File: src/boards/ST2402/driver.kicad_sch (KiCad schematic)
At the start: 61 parts, among them J15 Screw_Terminal_01x01, J16 Screw_Terminal_01x01, J17 Screw_Terminal_01x01, J9 Screw_Terminal_01x02, Q1 STB100N10F7, Q2 STB100N10F7, U2 LM317L_SOT-89

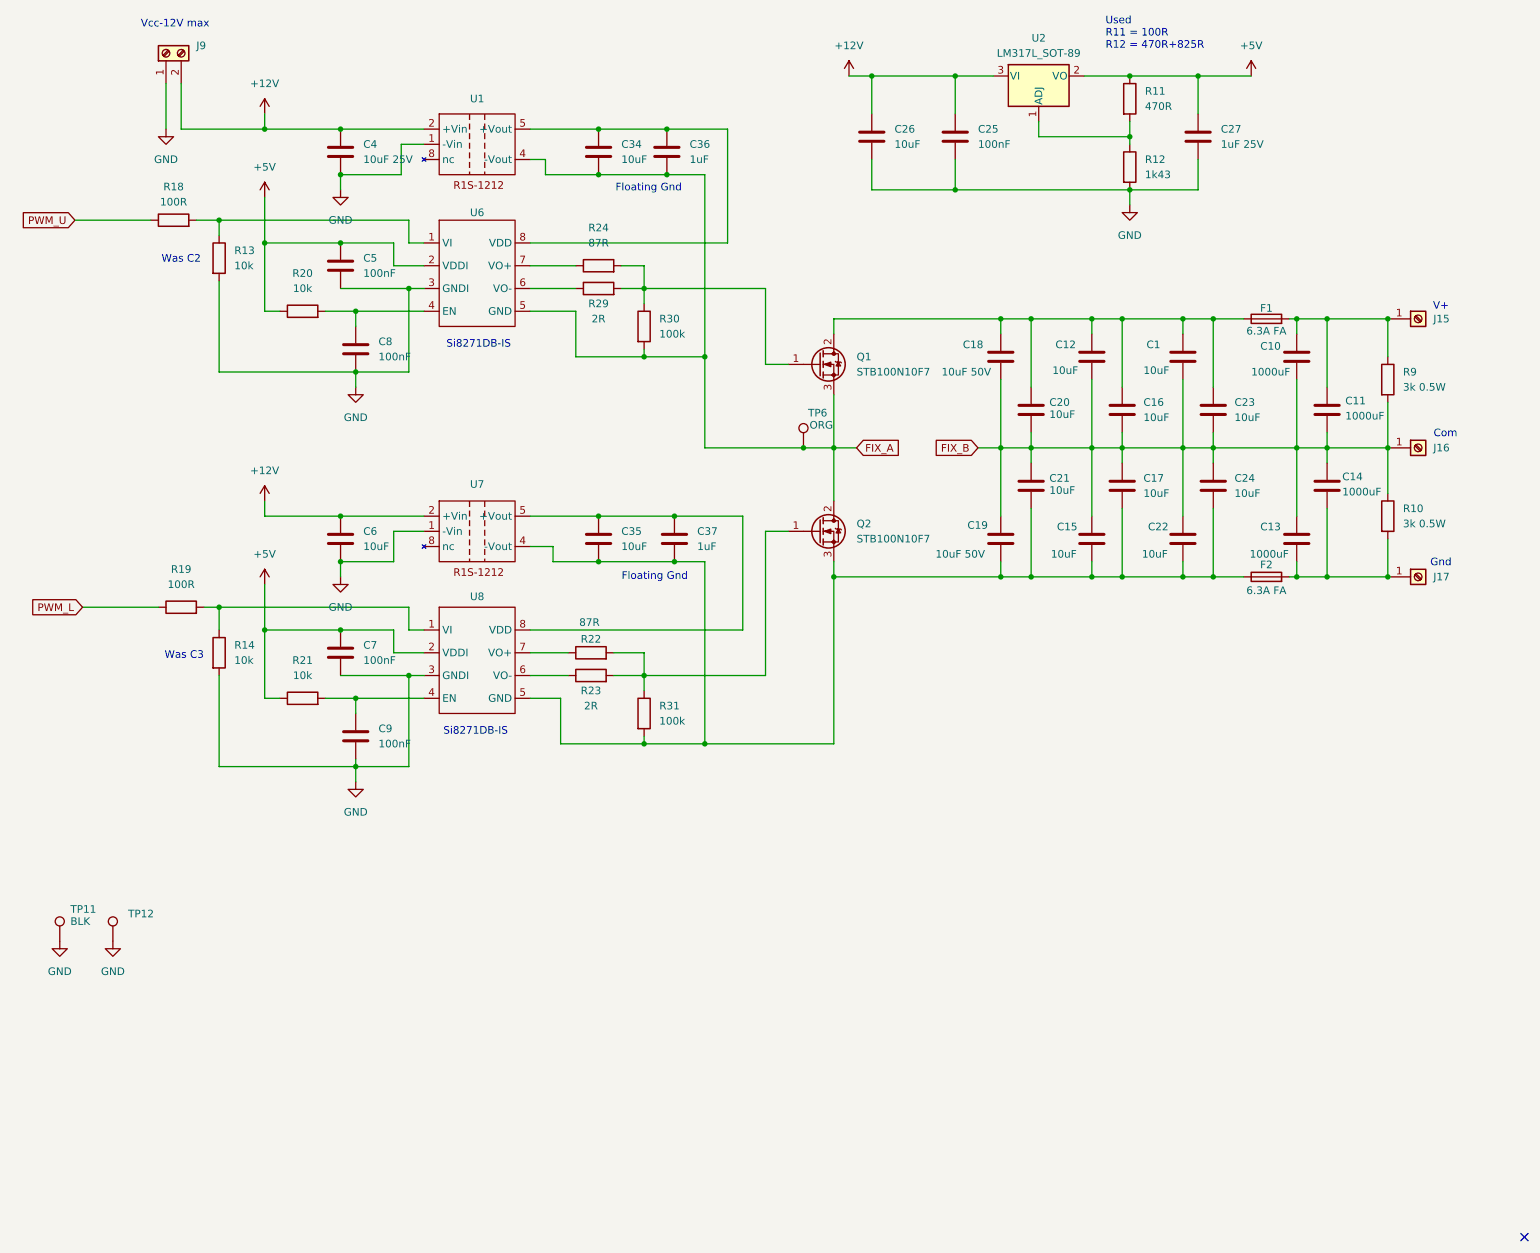
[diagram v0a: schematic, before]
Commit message: Added Mouser part numbers
Updated BOM and schematic with Mouser part numbers
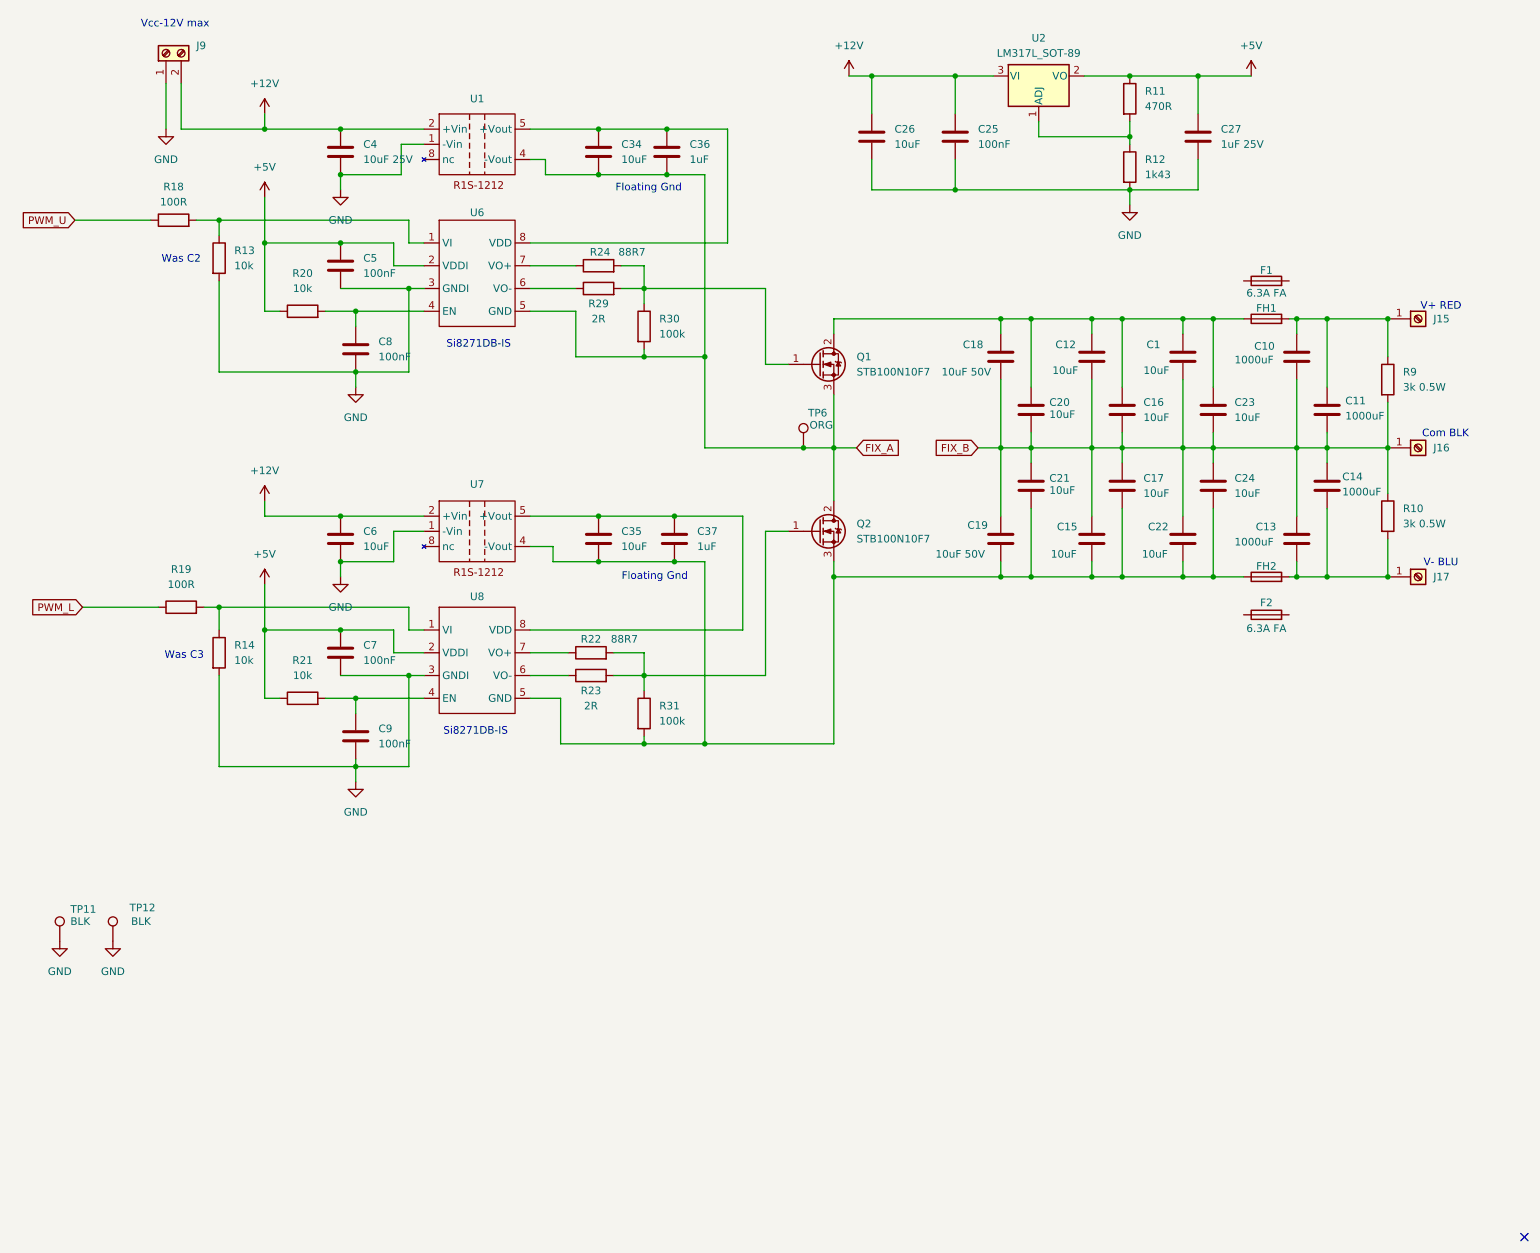
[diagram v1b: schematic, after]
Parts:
- added FH1, FH2: 6.3A FA, Fuse:Fuseholder_TR5_Littelfuse_No560_No460, symbol Device:Fuse
- C1, C12, C15, C16, C17, C18, C19, C20, C21, C22, C23, C24: Mouser ordercode (none) -> 603-CC210KKX7R9BB106
- C10, C11, C13, C14: Mouser ordercode (none) -> 710-861141085021
- C25, C5, C7, C8, C9: Mouser ordercode (none) -> 710-885012207098
- C26, C34, C35, C4, C6: Mouser ordercode (none) -> 710-885012108022
- C27, C36, C37: Mouser ordercode (none) -> 710-85012207103
- F1, F2: Mouser ordercode (none) -> 576-37416300000
- J15: value Screw_Terminal_01x01 -> ~; Mouser ordercode (none) -> 164-6219
- J16: value Screw_Terminal_01x01 -> ~; Mouser ordercode (none) -> 163-6218
- J17: value Screw_Terminal_01x01 -> ~; Mouser ordercode (none) -> 164-7120
- J9: Mouser ordercode (none) -> 490-TB006-508-02BE
- Q1, Q2: Mouser ordercode (none) -> 511-STP100N10F7
- R10, R9: Mouser ordercode (none) -> 603-RSF100JB-73-3K
- R11: Mouser ordercode (none) -> 603-RC0805FR-07470RL
- R12: Mouser ordercode (none) -> 603-RC0805FR-071K43L
- R13, R14, R20, R21: Mouser ordercode (none) -> 603-RC0805FR-0710KL
- R18, R19: Mouser ordercode (none) -> 603-RC0805FR-07100RL
- R22, R24: value 87R -> 88R7; Mouser ordercode (none) -> 603-RC0805FR-0788R7L
- R23, R29: Mouser ordercode (none) -> 603-RC0805FR-072RL
- R30, R31: Mouser ordercode (none) -> 603-RC0805FR-07100KL
- TP11: Mouser ordercode (none) -> 534-5011
- TP12: value TestPoint -> BLK; Mouser ordercode (none) -> 534-5011
- TP6: Mouser ordercode (none) -> 534-5013
- U1, U7: Mouser ordercode (none) -> 919-R1S-1212
- U2: Mouser ordercode (none) -> 595-LM317LCPK
- U6, U8: Mouser ordercode (none) -> 634-Si8271DB-IS
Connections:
- net at C15.2, C17.2, C19.2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: now also FH2.1; no longer F2.1
- net at C1.1, C12.1, C16.1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: now also FH1.1; no longer F1.1
- net at C13.2, C14.2, J17.1 (Pin_1)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: now also FH2.2; no longer F2.2
- net at C10.1, C11.1, J15.1 (Pin_1)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: now also FH1.2; no longer F1.2
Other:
- note added: "Com BLK"
- note added: "V+ RED"
- note added: "V- BLU"
- note removed: "Com"
- note removed: "Gnd"
- note removed: "Used R11 = 100R R12 = 470R+825R"
- note removed: "V+"
- moved on the sheet: F1, F2
